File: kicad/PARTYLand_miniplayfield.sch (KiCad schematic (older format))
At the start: 69 parts, among them P1 CONN_6, U1 74HC595, U2 74HC595, U3 74HC595, U4 74HC595

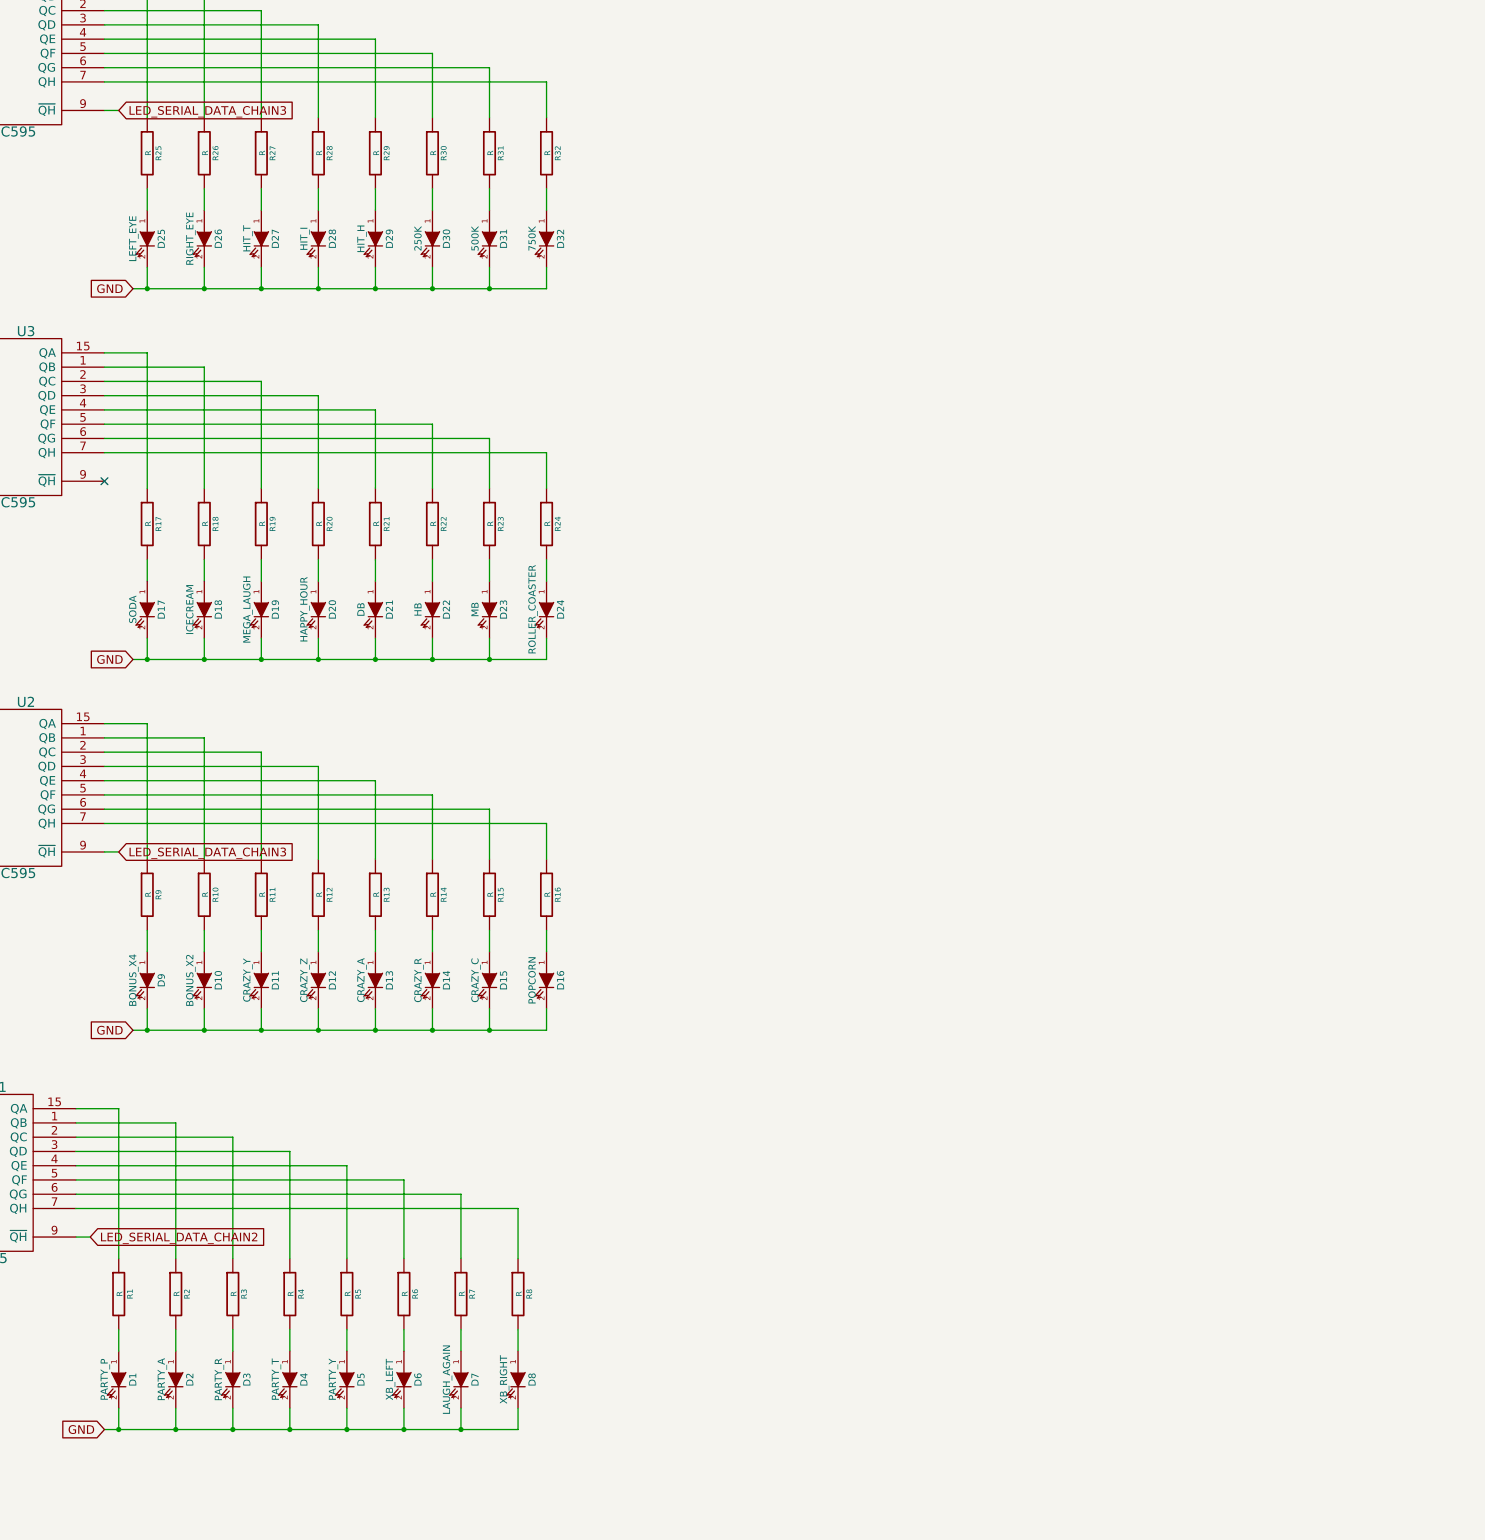
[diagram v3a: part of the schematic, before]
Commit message: Finished placing all LEDs in the miniplayfield schematics and pcb layout. Also added propper PCB cut edges and ground planes for copper fill.
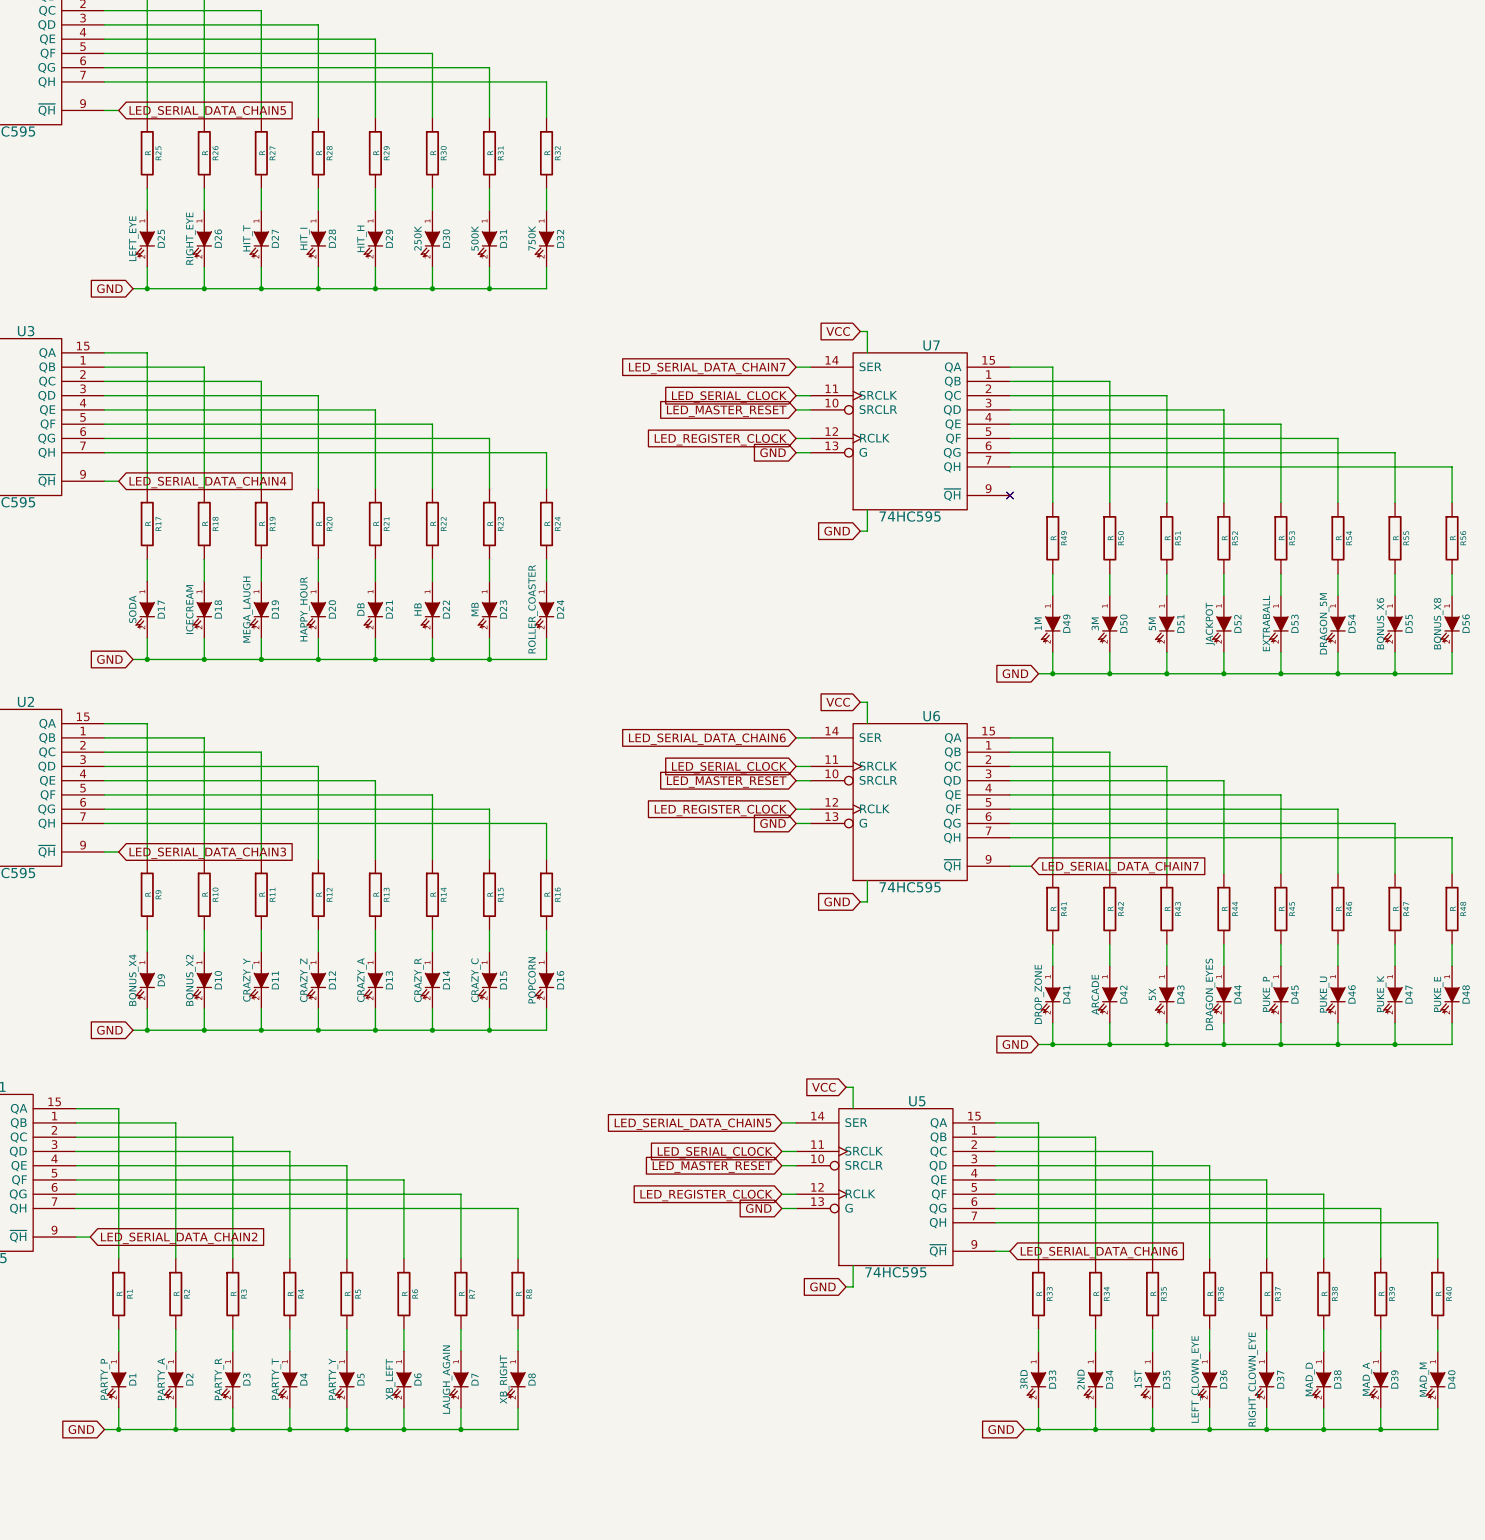
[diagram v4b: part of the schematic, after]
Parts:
- added D33: 3RD, LEDs:LED-3MM, symbol LED
- added D34: 2ND, LEDs:LED-3MM, symbol LED
- added D35: 1ST, LEDs:LED-3MM, symbol LED
- added D36: LEFT_CLOWN_EYE, LEDs:LED-3MM, symbol LED
- added D37: RIGHT_CLOWN_EYE, LEDs:LED-3MM, symbol LED
- added D38: MAD_D, LEDs:LED-3MM, symbol LED
- added D39: MAD_A, LEDs:LED-3MM, symbol LED
- added D40: MAD_M, LEDs:LED-3MM, symbol LED
- added D41: DROP_ZONE, LEDs:LED-3MM, symbol LED
- added D42: ARCADE, LEDs:LED-3MM, symbol LED
- added D43: 5X, LEDs:LED-3MM, symbol LED
- added D44: DRAGON_EYES, LEDs:LED-3MM, symbol LED
- added D45: PUKE_P, LEDs:LED-3MM, symbol LED
- added D46: PUKE_U, LEDs:LED-3MM, symbol LED
- added D47: PUKE_K, LEDs:LED-3MM, symbol LED
- added D48: PUKE_E, LEDs:LED-3MM, symbol LED
- added D49: 1M, LEDs:LED-3MM, symbol LED
- added D50: 3M, LEDs:LED-3MM, symbol LED
- added D51: 5M, LEDs:LED-3MM, symbol LED
- added D52: JACKPOT, LEDs:LED-3MM, symbol LED
- added D53: EXTRABALL, LEDs:LED-3MM, symbol LED
- added D54: DRAGON_5M, LEDs:LED-3MM, symbol LED
- added D55: BONUS_X6, LEDs:LED-3MM, symbol LED
- added D56: BONUS_X8, LEDs:LED-3MM, symbol LED
- added R33, R34, R35, R36, R37, R38, R39, R40, R41, R42, R43, R44, R45, R46, R47, R48, R49, R50, R51, R52, R53, R54, R55, R56: R, Discret:R3, symbol R
- added U5, U6, U7: 74HC595, Sockets_DIP:DIP-16__300_ELL, symbol 74HC595
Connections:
- net +5V: now also U5.16 (VCC), U6.16 (VCC), U7.16 (VCC)
- net GND: now also D33.2 (K), D34.2 (K), D35.2 (K), D36.2 (K), D37.2 (K), D38.2 (K), D39.2 (K), D40.2 (K), D41.2 (K), D42.2 (K), D43.2 (K), D44.2 (K), D45.2 (K), D46.2 (K), D47.2 (K), D48.2 (K), D49.2 (K), D50.2 (K), D51.2 (K), D52.2 (K), D53.2 (K), D54.2 (K), D55.2 (K), D56.2 (K), U5.13 (G), U5.8 (GND), U6.13 (G), U6.8 (GND), U7.13 (G), U7.8 (GND)
- net LED_MASTER_RESET: now also U5.10 (SRCLR), U6.10 (SRCLR), U7.10 (SRCLR)
- net LED_REGISTER_CLOCK: now also U5.12 (RCLK), U6.12 (RCLK), U7.12 (RCLK)
- net LED_SERIAL_CLOCK: now also U5.11 (SRCLK), U6.11 (SRCLK), U7.11 (SRCLK)
- net LED_SERIAL_DATA_CHAIN3: no longer U4.9 (~QH)
- net LED_SERIAL_DATA_CHAIN4: now also U3.9 (~QH)
- new net: R34.1, U5.1 (QB)
- new net: R33.1, U5.15 (QA)
- new net: R35.1, U5.2 (QC)
- new net: R36.1, U5.3 (QD)
- new net: R37.1, U5.4 (QE)
- new net: R38.1, U5.5 (QF)
- new net: R39.1, U5.6 (QG)
- new net: R40.1, U5.7 (QH)
- new net: D36.1 (A), R36.2
- new net: D37.1 (A), R37.2
- new net: D38.1 (A), R38.2
- new net: D35.1 (A), R35.2
- new net: D34.1 (A), R34.2
- new net: D33.1 (A), R33.2
- new net: D39.1 (A), R39.2
- new net: D40.1 (A), R40.2
- new net: R42.1, U6.1 (QB)
- new net: R41.1, U6.15 (QA)
- new net: R43.1, U6.2 (QC)
- new net: R44.1, U6.3 (QD)
- new net: R45.1, U6.4 (QE)
- new net: R46.1, U6.5 (QF)
- new net: R47.1, U6.6 (QG)
- new net: R48.1, U6.7 (QH)
- new net: D44.1 (A), R44.2
- new net: D45.1 (A), R45.2
- new net: D46.1 (A), R46.2
- new net: D43.1 (A), R43.2
- new net: D42.1 (A), R42.2
- new net: D41.1 (A), R41.2
- new net: D47.1 (A), R47.2
- new net: D48.1 (A), R48.2
- new net: R50.1, U7.1 (QB)
- new net: R49.1, U7.15 (QA)
- new net: R51.1, U7.2 (QC)
- new net: R52.1, U7.3 (QD)
- new net: R53.1, U7.4 (QE)
- new net: R54.1, U7.5 (QF)
- new net: R55.1, U7.6 (QG)
- new net: R56.1, U7.7 (QH)
- new net: D52.1 (A), R52.2
- new net: D53.1 (A), R53.2
- new net: D54.1 (A), R54.2
- new net: D51.1 (A), R51.2
- new net: D50.1 (A), R50.2
- new net: D49.1 (A), R49.2
- new net: D55.1 (A), R55.2
- new net: D56.1 (A), R56.2
- new net LED_SERIAL_DATA_CHAIN5: U4.9 (~QH), U5.14 (SER)
- new net LED_SERIAL_DATA_CHAIN6: U5.9 (~QH), U6.14 (SER)
- new net LED_SERIAL_DATA_CHAIN7: U6.9 (~QH), U7.14 (SER)

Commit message: wip: tracing the minipinball PCB
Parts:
- added R57, R58, R59, R60, R61, R62, R63, R64: R, Discret:R3, symbol R
- added SW1, SW2, SW3, SW4, SW5, SW6, SW7, SW8: SW_PUSH, symbol SW_PUSH
- added U8: 74LS165, symbol 74LS165
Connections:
- net +5V: now also SW1.1, SW2.1, SW3.1, SW4.1, SW5.1, SW6.1, SW7.1, SW8.1, U8.16 (VCC)
- net GND: now also R57.2, R58.2, R59.2, R60.2, R61.2, R62.2, R63.2, R64.2, U8.15 (CE), U8.8 (GND)
- new net: R57.1, SW1.2, U8.11 (P0)
- new net: R58.1, SW2.2, U8.12 (P1)
- new net: R59.1, SW3.2, U8.13 (P2)
- new net: R60.1, SW4.2, U8.14 (P3)
- new net: R61.1, SW5.2, U8.3 (P4)
- new net: R62.1, SW6.2, U8.4 (P5)
- new net: R63.1, SW7.2, U8.5 (P6)
- new net: R64.1, SW8.2, U8.6 (P7)
- new net SWITCH_REGISTER_CLOCK: U8.1 (Pl)
- new net SWITCH_SERIAL_CLOCK: U8.2 (CP)
- new net SWITCH_SERIAL_DATA: U8.9 (Q7)
- no-connect marks 1 -> 3

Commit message: * changing the connector size to also carry the switch control signals * resizing all labels to avoid overlap of neighbouring labels
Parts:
- P1: value CONN_6 -> CONN_10; footprint Pin_Headers:Pin_Header_Straight_1x06 -> Pin_Headers:Pin_Header_Angled_1x10; symbol CONN_6 -> CONN_10
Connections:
- net +5V: now also P1.10 (P10); no longer P1.6
- net GND: now also P1.5 (P5), U8.10 (Ds)
- net LED_MASTER_RESET: now also P1.6 (P6); no longer P1.2
- net LED_REGISTER_CLOCK: now also P1.7 (P7); no longer P1.3
- net LED_SERIAL_CLOCK: now also P1.9 (P9); no longer P1.5
- net LED_SERIAL_DATA: now also P1.8 (P8); no longer P1.4
- net SWITCH_REGISTER_CLOCK: now also P1.2 (P2)
- net SWITCH_SERIAL_CLOCK: now also P1.4 (P4)
- net SWITCH_SERIAL_DATA: now also P1.3 (P3)
- no-connect marks 3 -> 2
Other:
- moved on the sheet: D33, D34, D35, D36, D37, D38, D39, D40, R33, R34, R35, R36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

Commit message: work in progress...
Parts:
- SW1, SW2, SW3, SW4, SW5, SW6, SW7, SW8: footprint (none) -> Discret:SW_PUSH_SMALL
- U8: footprint (none) -> Sockets_DIP:DIP-16__300_ELL
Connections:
- net GND: no longer U8.10 (Ds)
- new net SWITCH_SERIAL_DATA_CHAIN1: U8.10 (Ds)
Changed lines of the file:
@@
 F 0 "SW8" H 17650 12760 50  0000 C CNN
 F 1 "SW_PUSH" H 17500 12570 50  0000 C CNN
-F 2 "" H 17500 12650 60  0000 C CNN
+F 2 "Discret:SW_PUSH_SMALL" H 17500 12650 60  0001 C CNN
 F 3 "" H 17500 12650 60  0000 C CNN
 	1    17500 12650
@@
 F 0 "SW7" H 17250 12760 50  0000 C CNN
 F 1 "SW_PUSH" H 17100 12570 50  0000 C CNN
-F 2 "" H 17100 12650 60  0000 C CNN
+F 2 "Discret:SW_PUSH_SMALL" H 17100 12650 60  0001 C CNN
 F 3 "" H 17100 12650 60  0000 C CNN
 	1    17100 12650
@@
 F 0 "SW6" H 16850 12760 50  0000 C CNN
 F 1 "SW_PUSH" H 16700 12570 50  0000 C CNN
-F 2 "" H 16700 12650 60  0000 C CNN
+F 2 "Discret:SW_PUSH_SMALL" H 16700 12650 60  0001 C CNN
 F 3 "" H 16700 12650 60  0000 C CNN
 	1    16700 12650
@@
 F 0 "SW5" H 16450 12760 50  0000 C CNN
 F 1 "SW_PUSH" H 16300 12570 50  0000 C CNN
-F 2 "" H 16300 12650 60  0000 C CNN
+F 2 "Discret:SW_PUSH_SMALL" H 16300 12650 60  0001 C CNN
 F 3 "" H 16300 12650 60  0000 C CNN
 	1    16300 12650
@@
 F 0 "SW4" H 16050 12760 50  0000 C CNN
 F 1 "SW_PUSH" H 15900 12570 50  0000 C CNN
-F 2 "" H 15900 12650 60  0000 C CNN
+F 2 "Discret:SW_PUSH_SMALL" H 15900 12650 60  0001 C CNN
 F 3 "" H 15900 12650 60  0000 C CNN
 	1    15900 12650
@@
 F 0 "SW3" H 15650 12760 50  0000 C CNN
 F 1 "SW_PUSH" H 15500 12570 50  0000 C CNN
-F 2 "" H 15500 12650 60  0000 C CNN
+F 2 "Discret:SW_PUSH_SMALL" H 15500 12650 60  0001 C CNN
 F 3 "" H 15500 12650 60  0000 C CNN
 	1    15500 12650
@@
 F 0 "SW2" H 15250 12760 50  0000 C CNN
 F 1 "SW_PUSH" H 15100 12570 50  0000 C CNN
-F 2 "" H 15100 12650 60  0000 C CNN
+F 2 "Discret:SW_PUSH_SMALL" H 15100 12650 60  0001 C CNN
 F 3 "" H 15100 12650 60  0000 C CNN
 	1    15100 12650
@@
 F 0 "SW1" H 14850 12760 50  0000 C CNN
 F 1 "SW_PUSH" H 14700 12570 50  0000 C CNN
-F 2 "" H 14700 12650 60  0000 C CNN
+F 2 "Discret:SW_PUSH_SMALL" H 14700 12650 60  0001 C CNN
 F 3 "" H 14700 12650 60  0000 C CNN
 	1    14700 12650
@@
 F 0 "U8" H 19950 13500 60  0000 C CNN
 F 1 "74LS165" H 19950 13300 60  0000 C CNN
-F 2 "" H 19800 13550 60  0000 C CNN
+F 2 "Sockets_DIP:DIP-16__300_ELL" H 19800 13550 60  0001 C CNN
 F 3 "" H 19800 13550 60  0000 C CNN
 	1    19800 13550
@@
 GND
 Text GLabel 18950 12950 0    39   Input ~ 0
-GND
-Wire Wire Line
-	1400 15300 1450 15300
-Wire Wire Line
-	1450 15300 1500 15300
+SWITCH_SERIAL_DATA_CHAIN1
+Wire Wire Line
+	1400 15300 1500 15300
 Wire Wire Line
 	1500 14600 1400 14600
@@
 	1400 14500 1500 14500
 Wire Wire Line
-	1400 14400 1450 14400
-Wire Wire Line
-	1450 14400 1500 14400
+	1400 14400 1500 14400
 Wire Wire Line
 	1400 14700 1500 14700
@@
 	3750 14400 3750 14550
 Wire Wire Line
-	3650 14550 3750 14550
-Wire Wire Line
-	3750 14550 4150 14550
-Wire Wire Line
-	4150 14550 4550 14550
-Wire Wire Line
-	4550 14550 4950 14550
-Wire Wire Line
-	4950 14550 5350 14550
-Wire Wire Line
-	5350 14550 5750 14550
-Wire Wire Line
-	5750 14550 6150 14550
-Wire Wire Line
-	6150 14550 6550 14550
+	3650 14550 6550 14550
 Wire Wire Line
 	6550 14550 6550 14400
@@
 	6550 14000 6550 13850
 Wire Wire Line
-	1450 14100 1450 14300
-Wire Wire Line
-	1450 14300 1450 14400
+	1450 14100 1450 14400
 Connection ~ 1450 14400
 Wire Wire Line
@@
 	2400 13450 2450 13450
 Wire Wire Line
-	1450 14900 1450 15300
-Wire Wire Line
-	1450 15300 1450 15450
-Wire Wire Line
-	1450 15450 1450 15650
+	1450 14900 1450 15650
 Connection ~ 1450 15300
 Wire Wire Line
 	3950 11600 3950 11750
 Wire Wire Line
-	3850 11750 3950 11750
-Wire Wire Line
-	3950 11750 4350 11750
-Wire Wire Line
-	4350 11750 4750 11750
-Wire Wire Line
-	4750 11750 5150 11750
-Wire Wire Line
-	5150 11750 5550 11750
-Wire Wire Line
-	5550 11750 5950 11750
-Wire Wire Line
-	5950 11750 6350 11750
-Wire Wire Line
-	6350 11750 6750 11750
+	3850 11750 6750 11750
 Wire Wire Line
 	6750 11750 6750 11600
@@
 	3950 9000 3950 9150
 Wire Wire Line
-	3850 9150 3950 9150
-Wire Wire Line
-	3950 9150 4350 9150
-Wire Wire Line
-	4350 9150 4750 9150
-Wire Wire Line
-	4750 9150 5150 9150
-Wire Wire Line
-	5150 9150 5550 9150
-Wire Wire Line
-	5550 9150 5950 9150
-Wire Wire Line
-	5950 9150 6350 9150
-Wire Wire Line
-	6350 9150 6750 9150
+	3850 9150 6750 9150
 Wire Wire Line
 	6750 9150 6750 9000
@@
 	3950 6400 3950 6550
 Wire Wire Line
-	3850 6550 3950 6550
-Wire Wire Line
-	3950 6550 4350 6550
-Wire Wire Line
-	4350 6550 4750 6550
-Wire Wire Line
-	4750 6550 5150 6550
-Wire Wire Line
-	5150 6550 5550 6550
-Wire Wire Line
-	5550 6550 5950 6550
-Wire Wire Line
-	5950 6550 6350 6550
-Wire Wire Line
-	6350 6550 6750 6550
+	3850 6550 6750 6550
 Wire Wire Line
 	6750 6550 6750 6400
@@
 	10200 14550 10200 14700
 Wire Wire Line
-	10100 14700 10200 14700
-Wire Wire Line
-	10200 14700 10600 14700
-Wire Wire Line
-	10600 14700 11000 14700
-Wire Wire Line
-	11000 14700 11400 14700
-Wire Wire Line
-	11400 14700 11800 14700
-Wire Wire Line
-	11800 14700 12200 14700
-Wire Wire Line
-	12200 14700 12600 14700
-Wire Wire Line
-	12600 14700 13000 14700
+	10100 14700 13000 14700
 Wire Wire Line
 	13000 14700 13000 14550
@@
 	10300 11700 10300 11850
 Wire Wire Line
-	10200 11850 10300 11850
-Wire Wire Line
-	10300 11850 10700 11850
-Wire Wire Line
-	10700 11850 11100 11850
-Wire Wire Line
-	11100 11850 11500 11850
-Wire Wire Line
-	11500 11850 11900 11850
-Wire Wire Line
-	11900 11850 12300 11850
-Wire Wire Line
-	12300 11850 12700 11850
-Wire Wire Line
-	12700 11850 13100 11850
+	10200 11850 13100 11850
 Wire Wire Line
 	13100 11850 13100 11700
@@
 	10300 9100 10300 9250
 Wire Wire Line
-	10200 9250 10300 9250
-Wire Wire Line
-	10300 9250 10700 9250
-Wire Wire Line
-	10700 9250 11100 9250
-Wire Wire Line
-	11100 9250 11500 9250
-Wire Wire Line
-	11500 9250 11900 9250
-Wire Wire Line
-	11900 9250 12300 9250
-Wire Wire Line
-	12300 9250 12700 9250
-Wire Wire Line
-	12700 9250 13100 9250
+	10200 9250 13100 9250
 Wire Wire Line
 	13100 9250 13100 9100
@@
 	14700 12200 14700 12350
 Wire Wire Line
-	14550 12200 14700 12200
-Wire Wire Line
-	14700 12200 15100 12200
-Wire Wire Line
-	15100 12200 15500 12200
-Wire Wire Line
-	15500 12200 15900 12200
-Wire Wire Line
-	15900 12200 16300 12200
-Wire Wire Line
-	16300 12200 16700 12200
-Wire Wire Line
-	16700 12200 17100 12200
-Wire Wire Line
-	17100 12200 17500 12200
+	14550 12200 17500 12200
 Connection ~ 17500 13750
 Connection ~ 17100 13650
@@
 	17500 13750 19100 13750
 Wire Wire Line
-	17500 12950 17500 13750
-Wire Wire Line
-	17500 13750 17500 13850
-Wire Wire Line
-	17100 12950 17100 13650
-Wire Wire Line
-	17100 13650 17100 13850
+	17500 12950 17500 13850
+Wire Wire Line
+	17100 12950 17100 13850
 Wire Wire Line
 	19100 13650 17100 13650
@@
 	16700 13550 19100 13550
 Wire Wire Line
-	16700 12950 16700 13550
-Wire Wire Line
-	16700 13550 16700 13850
-Wire Wire Line
-	16300 12950 16300 13450
-Wire Wire Line
-	16300 13450 16300 13850
+	16700 12950 16700 13850
+Wire Wire Line
+	16300 12950 16300 13850
 Wire Wire Line
 	19100 13450 16300 13450
@@
 	15900 13350 19100 13350
 Wire Wire Line
-	15900 12950 15900 13350
-Wire Wire Line
-	15900 13350 15900 13850
-Wire Wire Line
-	15500 12950 15500 13250
-Wire Wire Line
-	15500 13250 15500 13850
+	15900 12950 15900 13850
+Wire Wire Line
+	15500 12950 15500 13850
 Wire Wire Line
 	19100 13250 15500 13250
@@
 	15100 13150 19100 13150
 Wire Wire Line
-	15100 12950 15100 13150
-Wire Wire Line
-	15100 13150 15100 13850
-Wire Wire Line
-	14700 12950 14700 13050
-Wire Wire Line
-	14700 13050 14700 13850
+	15100 12950 15100 13850
+Wire Wire Line
+	14700 12950 14700 13850
 Wire Wire Line
 	19100 13050 14700 13050
@@
 	17500 14500 17500 14350
 Wire Wire Line
-	14600 14500 14700 14500
-Wire Wire Line
-	14700 14500 15100 14500
-Wire Wire Line
-	15100 14500 15500 14500
-Wire Wire Line
-	15500 14500 15900 14500
-Wire Wire Line
-	15900 14500 16300 14500
-Wire Wire Line
-	16300 14500 16700 14500
-Wire Wire Line
-	16700 14500 17100 14500
-Wire Wire Line
-	17100 14500 17500 14500
+	14600 14500 17500 14500
 Wire Wire Line
 	14700 14350 14700 14500
